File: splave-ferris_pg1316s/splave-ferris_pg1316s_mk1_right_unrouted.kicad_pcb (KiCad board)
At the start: 2 copper layers, 117.9 x 85.9 mm, 37 parts

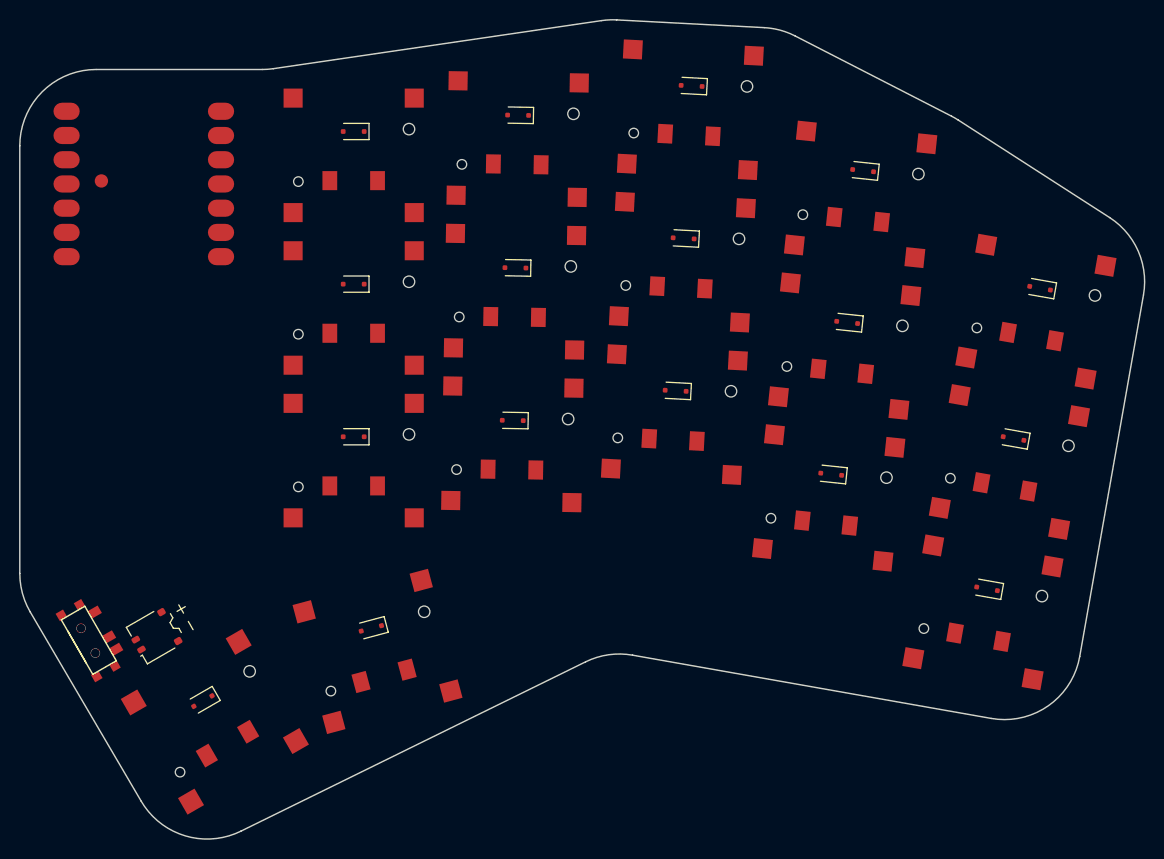
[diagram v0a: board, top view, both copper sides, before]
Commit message: Add stablizer holes to PG1316S footprint, regenerate PCB files.
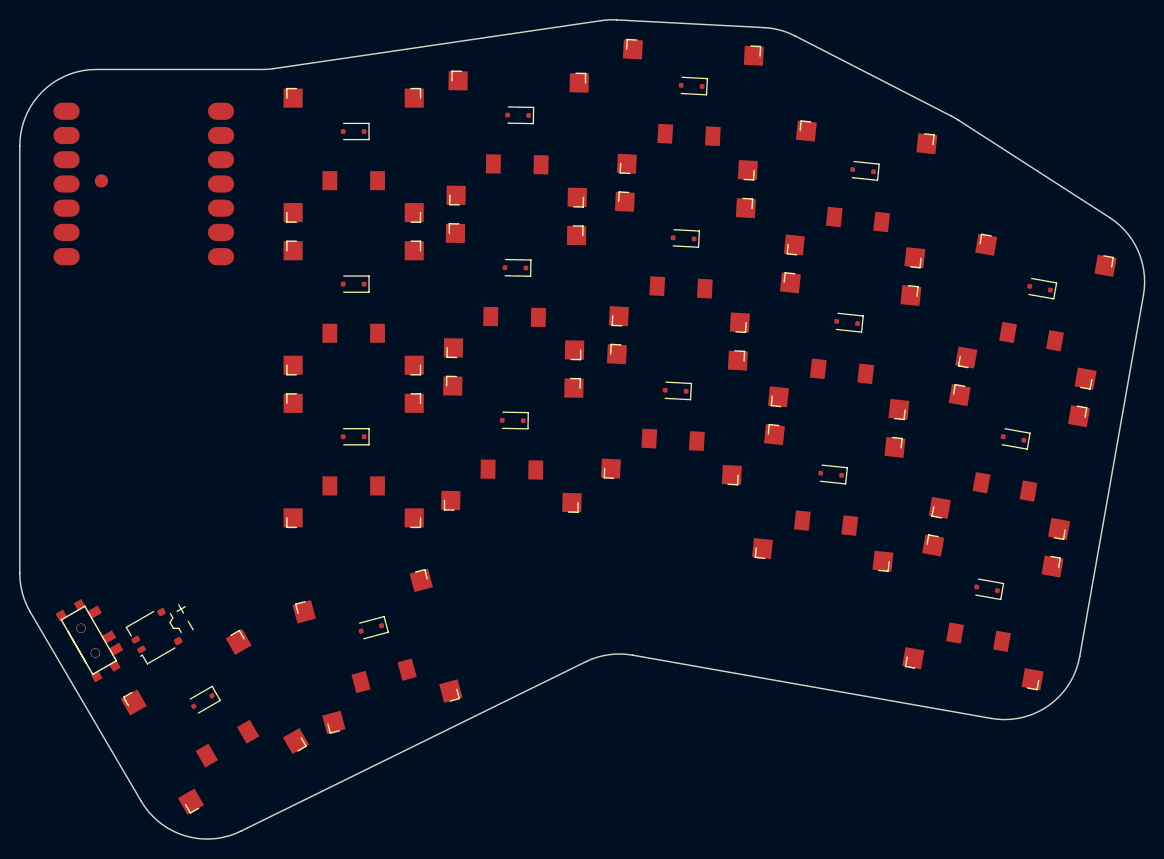
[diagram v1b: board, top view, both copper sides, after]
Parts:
- S1, S10, S11, S12, S13, S14, S15, S16, S17, S2, S3, S4, S5, S6, S7, S8, S9: footprint CPG1316S01D02_mikeholscher -> PG1316S
